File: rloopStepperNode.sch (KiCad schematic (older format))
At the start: 0 parts

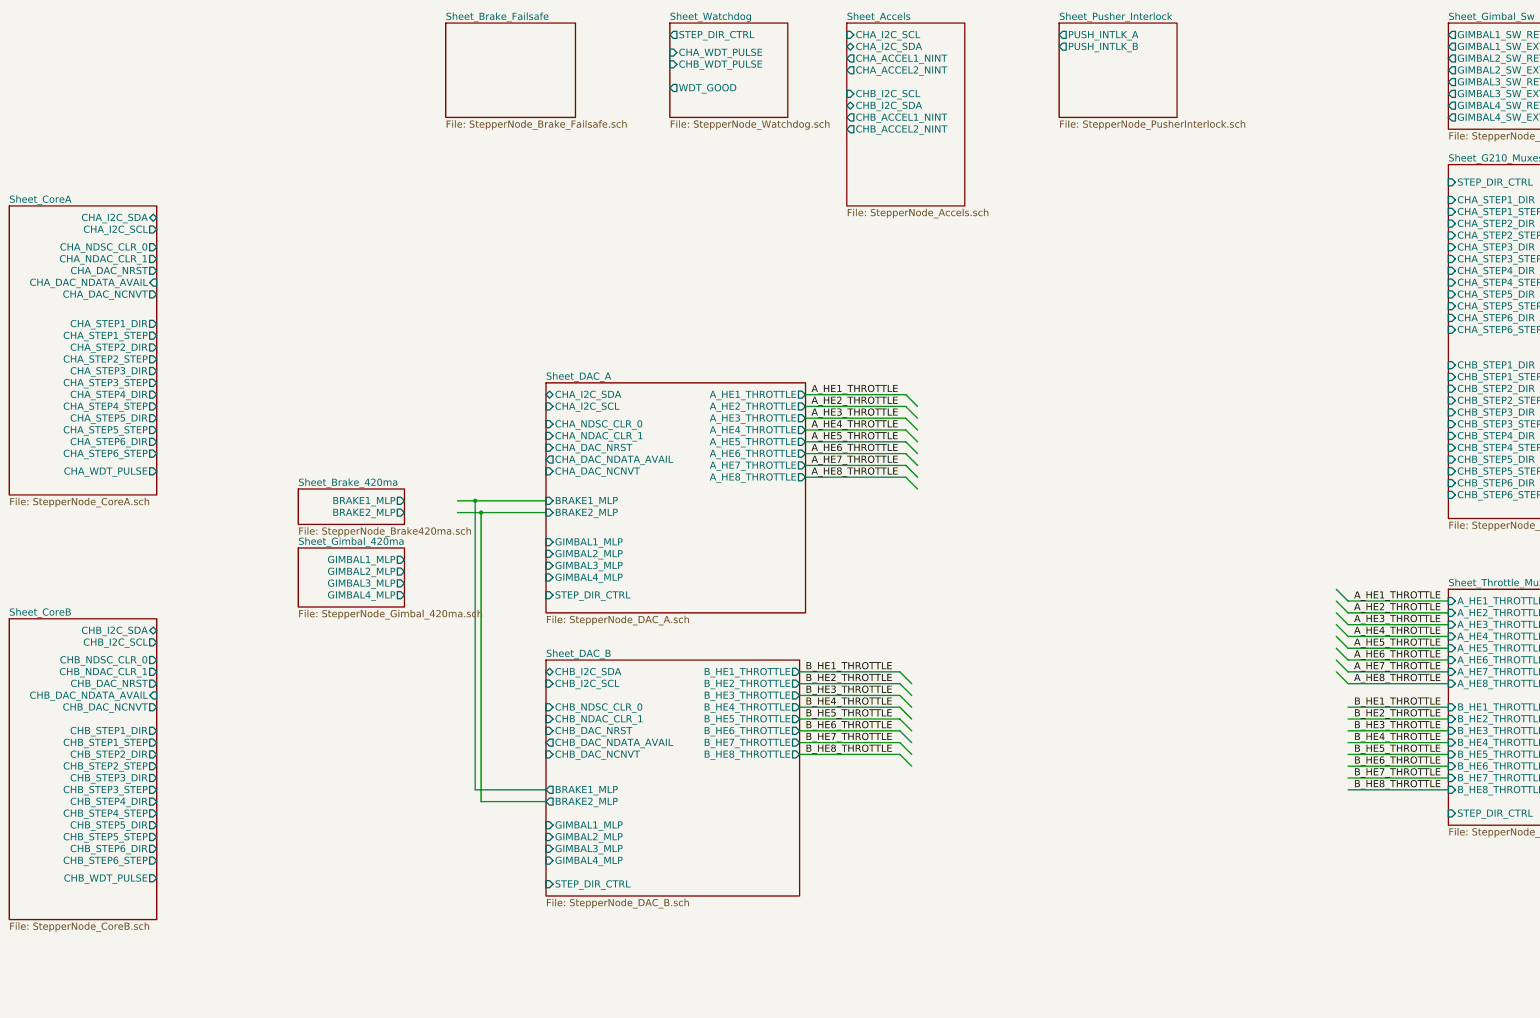
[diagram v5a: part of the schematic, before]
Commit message: Added Aux Prop Interface Sheet
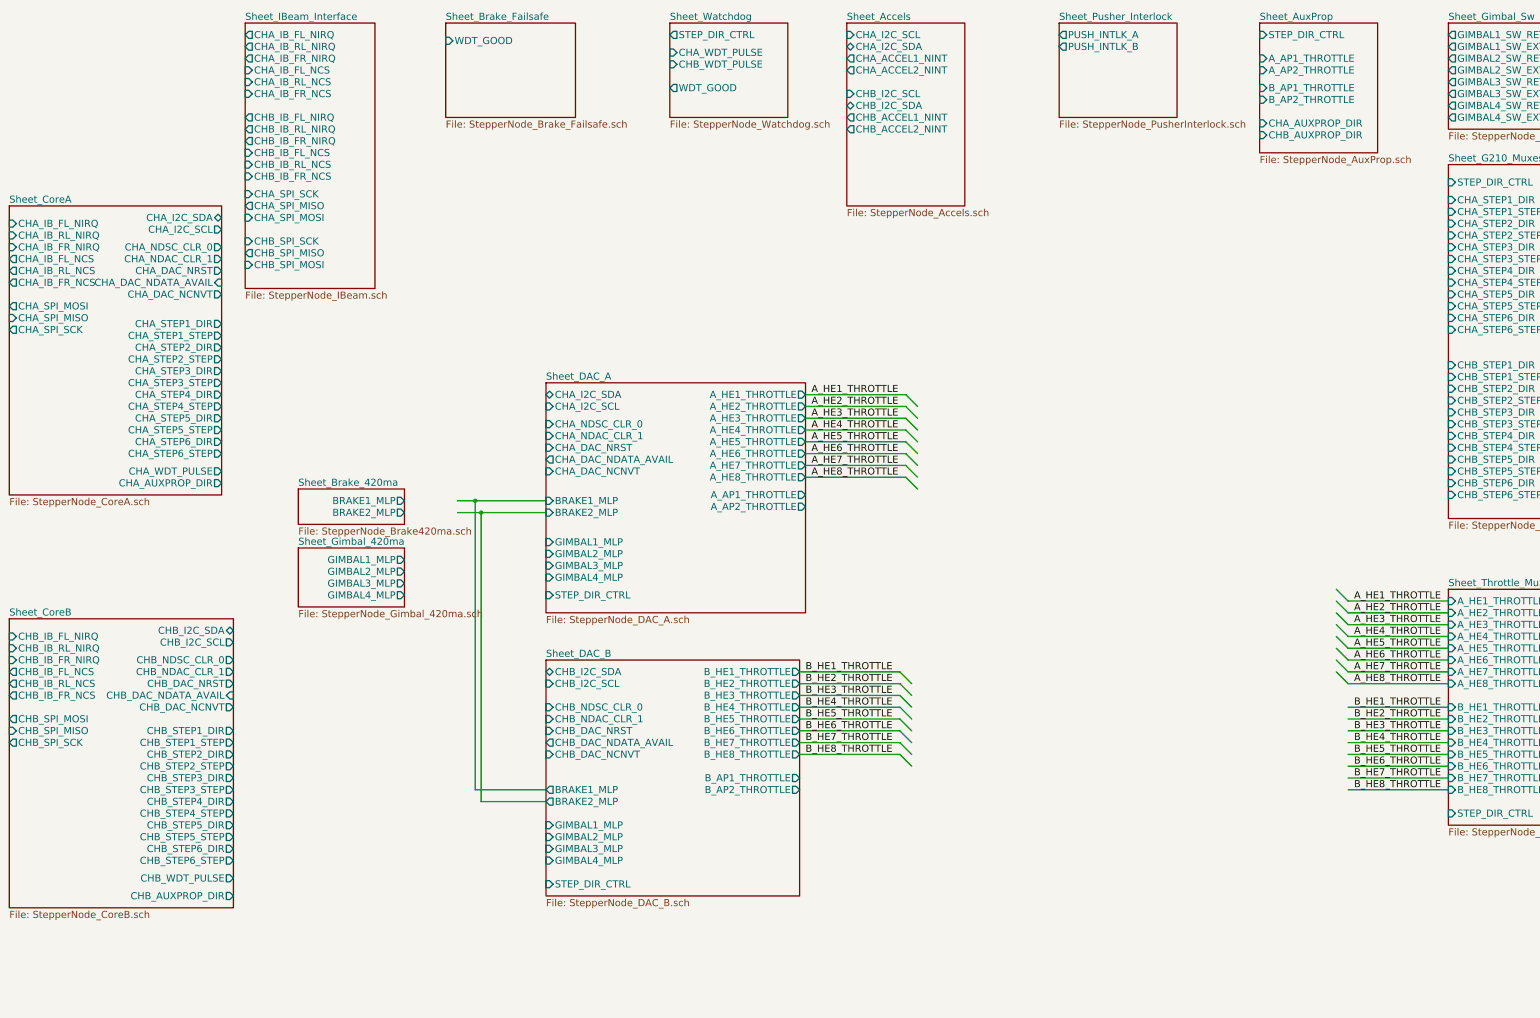
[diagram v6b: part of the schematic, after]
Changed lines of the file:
@@
 $Descr A3 16535 11693
 encoding utf-8
-Sheet 1 14
+Sheet 1 16
 Title "Top Level"
 Date ""
@@
 F22 "GIMBAL4_MLP" I L 6550 5500 60
 F23 "STEP_DIR_CTRL" I L 6550 5650 60
+F24 "A_AP1_THROTTLE" O R 8750 4800 60
+F25 "A_AP2_THROTTLE" O R 8750 4900 60
 $EndSheet
 $Sheet
@@
 F22 "CHB_DAC_NDATA_AVAIL" O L 6550 6900 60
 F23 "CHB_DAC_NCNVT" I L 6550 7000 60
+F24 "B_AP1_THROTTLE" O R 8700 7200 60
+F25 "B_AP2_THROTTLE" O R 8700 7300 60
 $EndSheet
 Wire Wire Line
@@
 $EndSheet
 $Sheet
-S 2000 5850 1250 2550
+S 2000 5850 1900 2450
 U 57556833
 F0 "Sheet_CoreB" 60
 F1 "StepperNode_CoreB.sch" 60
-F2 "CHB_I2C_SDA" B R 3250 5950 60
-F3 "CHB_I2C_SCL" O R 3250 6050 60
-F4 "CHB_NDSC_CLR_0" O R 3250 6200 60
-F5 "CHB_NDAC_CLR_1" O R 3250 6300 60
-F6 "CHB_DAC_NRST" O R 3250 6400 60
-F7 "CHB_DAC_NDATA_AVAIL" I R 3250 6500 60
-F8 "CHB_DAC_NCNVT" O R 3250 6600 60
-F9 "CHB_STEP1_DIR" O R 3250 6800 60
-F10 "CHB_STEP1_STEP" O R 3250 6900 60
-F11 "CHB_STEP2_DIR" O R 3250 7000 60
-F12 "CHB_STEP2_STEP" O R 3250 7100 60
-F13 "CHB_STEP3_DIR" O R 3250 7200 60
-F14 "CHB_STEP3_STEP" O R 3250 7300 60
-F15 "CHB_STEP4_DIR" O R 3250 7400 60
-F16 "CHB_STEP4_STEP" O R 3250 7500 60
-F17 "CHB_STEP5_DIR" O R 3250 7600 60
-F18 "CHB_STEP5_STEP" O R 3250 7700 60
-F19 "CHB_STEP6_DIR" O R 3250 7800 60
-F20 "CHB_STEP6_STEP" O R 3250 7900 60
-F21 "CHB_WDT_PULSE" O R 3250 8050 60
-$EndSheet
-$Sheet
-S 2000 2350 1250 2450
+F2 "CHB_I2C_SDA" B R 3900 5950 60
+F3 "CHB_I2C_SCL" O R 3900 6050 60
+F4 "CHB_NDSC_CLR_0" O R 3900 6200 60
+F5 "CHB_NDAC_CLR_1" O R 3900 6300 60
+F6 "CHB_DAC_NRST" O R 3900 6400 60
+F7 "CHB_DAC_NDATA_AVAIL" I R 3900 6500 60
+F8 "CHB_DAC_NCNVT" O R 3900 6600 60
+F9 "CHB_STEP1_DIR" O R 3900 6800 60
+F10 "CHB_STEP1_STEP" O R 3900 6900 60
+F11 "CHB_STEP2_DIR" O R 3900 7000 60
+F12 "CHB_STEP2_STEP" O R 3900 7100 60
+F13 "CHB_STEP3_DIR" O R 3900 7200 60
+F14 "CHB_STEP3_STEP" O R 3900 7300 60
+F15 "CHB_STEP4_DIR" O R 3900 7400 60
+F16 "CHB_STEP4_STEP" O R 3900 7500 60
+F17 "CHB_STEP5_DIR" O R 3900 7600 60
+F18 "CHB_STEP5_STEP" O R 3900 7700 60
+F19 "CHB_STEP6_DIR" O R 3900 7800 60
+F20 "CHB_STEP6_STEP" O R 3900 7900 60
+F21 "CHB_WDT_PULSE" O R 3900 8050 60
+F22 "CHB_IB_FL_NIRQ" I L 2000 6000 60
+F23 "CHB_IB_RL_NIRQ" I L 2000 6100 60
+F24 "CHB_IB_FR_NIRQ" I L 2000 6200 60
+F25 "CHB_IB_RL_NCS" O L 2000 6400 60
+F26 "CHB_IB_FR_NCS" O L 2000 6500 60
+F27 "CHB_IB_FL_NCS" O L 2000 6300 60
+F28 "CHB_SPI_MOSI" O L 2000 6700 60
+F29 "CHB_SPI_MISO" I L 2000 6800 60
+F30 "CHB_SPI_SCK" O L 2000 6900 60
+F31 "CHB_AUXPROP_DIR" O R 3900 8200 60
+$EndSheet
+$Sheet
+S 2000 2350 1800 2450
 U 57538643
 F0 "Sheet_CoreA" 60
 F1 "StepperNode_CoreA.sch" 60
-F2 "CHA_I2C_SDA" B R 3250 2450 60
-F3 "CHA_I2C_SCL" O R 3250 2550 60
-F4 "CHA_NDSC_CLR_0" O R 3250 2700 60
-F5 "CHA_NDAC_CLR_1" O R 3250 2800 60
-F6 "CHA_DAC_NRST" O R 3250 2900 60
-F7 "CHA_DAC_NDATA_AVAIL" I R 3250 3000 60
-F8 "CHA_DAC_NCNVT" O R 3250 3100 60
-F9 "CHA_STEP1_DIR" O R 3250 3350 60
-F10 "CHA_STEP1_STEP" O R 3250 3450 60
-F11 "CHA_STEP2_DIR" O R 3250 3550 60
-F12 "CHA_STEP2_STEP" O R 3250 3650 60
-F13 "CHA_STEP3_DIR" O R 3250 3750 60
-F14 "CHA_STEP3_STEP" O R 3250 3850 60
-F15 "CHA_STEP4_DIR" O R 3250 3950 60
-F16 "CHA_STEP4_STEP" O R 3250 4050 60
-F17 "CHA_STEP5_DIR" O R 3250 4150 60
-F18 "CHA_STEP5_STEP" O R 3250 4250 60
-F19 "CHA_STEP6_DIR" O R 3250 4350 60
-F20 "CHA_STEP6_STEP" O R 3250 4450 60
-F21 "CHA_WDT_PULSE" O R 3250 4600 60
+F2 "CHA_I2C_SDA" B R 3800 2450 60
+F3 "CHA_I2C_SCL" O R 3800 2550 60
+F4 "CHA_NDSC_CLR_0" O R 3800 2700 60
+F5 "CHA_NDAC_CLR_1" O R 3800 2800 60
+F6 "CHA_DAC_NRST" O R 3800 2900 60
+F7 "CHA_DAC_NDATA_AVAIL" I R 3800 3000 60
+F8 "CHA_DAC_NCNVT" O R 3800 3100 60
+F9 "CHA_STEP1_DIR" O R 3800 3350 60
+F10 "CHA_STEP1_STEP" O R 3800 3450 60
+F11 "CHA_STEP2_DIR" O R 3800 3550 60
+F12 "CHA_STEP2_STEP" O R 3800 3650 60
+F13 "CHA_STEP3_DIR" O R 3800 3750 60
+F14 "CHA_STEP3_STEP" O R 3800 3850 60
+F15 "CHA_STEP4_DIR" O R 3800 3950 60
+F16 "CHA_STEP4_STEP" O R 3800 4050 60
+F17 "CHA_STEP5_DIR" O R 3800 4150 60
+F18 "CHA_STEP5_STEP" O R 3800 4250 60
+F19 "CHA_STEP6_DIR" O R 3800 4350 60
+F20 "CHA_STEP6_STEP" O R 3800 4450 60
+F21 "CHA_WDT_PULSE" O R 3800 4600 60
+F22 "CHA_IB_FL_NIRQ" I L 2000 2500 60
+F23 "CHA_IB_RL_NIRQ" I L 2000 2600 60
+F24 "CHA_IB_FR_NIRQ" I L 2000 2700 60
+F25 "CHA_IB_RL_NCS" O L 2000 2900 60
+F26 "CHA_IB_FR_NCS" O L 2000 3000 60
+F27 "CHA_IB_FL_NCS" O L 2000 2800 60
+F28 "CHA_SPI_MOSI" O L 2000 3200 60
+F29 "CHA_SPI_MISO" I L 2000 3300 60
+F30 "CHA_SPI_SCK" O L 2000 3400 60
+F31 "CHA_AUXPROP_DIR" O R 3800 4700 60
 $EndSheet
 $Sheet
@@
 F0 "Sheet_Brake_Failsafe" 60
 F1 "StepperNode_Brake_Failsafe.sch" 60
+F2 "WDT_GOOD" I L 5700 950 60
+$EndSheet
+$Sheet
+S 4000 800  1100 2250
+U 5753F632
+F0 "Sheet_IBeam_Interface" 60
+F1 "StepperNode_IBeam.sch" 60
+F2 "CHA_IB_FL_NIRQ" O L 4000 900 60
+F3 "CHA_SPI_MOSI" I L 4000 2450 60
+F4 "CHA_SPI_MISO" O L 4000 2350 60
+F5 "CHA_SPI_SCK" I L 4000 2250 60
+F6 "CHA_IB_FL_NCS" I L 4000 1200 60
+F7 "CHA_IB_RL_NIRQ" O L 4000 1000 60
+F8 "CHA_IB_FR_NIRQ" O L 4000 1100 60
+F9 "CHA_IB_RL_NCS" I L 4000 1300 60
+F10 "CHA_IB_FR_NCS" I L 4000 1400 60
+F11 "CHB_IB_FL_NIRQ" O L 4000 1600 60
+F12 "CHB_IB_RL_NIRQ" O L 4000 1700 60
+F13 "CHB_IB_FR_NIRQ" O L 4000 1800 60
+F14 "CHB_IB_RL_NCS" I L 4000 2000 60
+F15 "CHB_IB_FR_NCS" I L 4000 2100 60
+F16 "CHB_IB_FL_NCS" I L 4000 1900 60
+F17 "CHB_SPI_MOSI" I L 4000 2850 60
+F18 "CHB_SPI_MISO" O L 4000 2750 60
+F19 "CHB_SPI_SCK" I L 4000 2650 60
+$EndSheet
+$Sheet
+S 12600 800  1000 1100
+U 575A7A12
+F0 "Sheet_AuxProp" 60
+F1 "StepperNode_AuxProp.sch" 60
+F2 "STEP_DIR_CTRL" I L 12600 900 60
+F3 "A_AP1_THROTTLE" I L 12600 1100 60
+F4 "B_AP1_THROTTLE" I L 12600 1350 60
+F5 "A_AP2_THROTTLE" I L 12600 1200 60
+F6 "B_AP2_THROTTLE" I L 12600 1450 60
+F7 "CHA_AUXPROP_DIR" I L 12600 1650 60
+F8 "CHB_AUXPROP_DIR" I L 12600 1750 60
 $EndSheet
 $EndSCHEMATC

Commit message: Netlist top level
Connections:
- net labels added: A_AP1_THROTTLE, A_AP2_THROTTLE, BRAKE1_MLP, BRAKE2_MLP, B_AP1_THROTTLE, B_AP2_THROTTLE, CHA_ACCEL1_NINT, CHA_ACCEL2_NINT, CHA_AUXPROP_DIR, CHA_DAC_NCNVT, CHA_DAC_NDATA_AVAIL, CHA_DAC_NRST, CHA_I2C_SCL, CHA_I2C_SDA, CHA_IB_FL_NCS, CHA_IB_FL_NIRQ, CHA_IB_FR_NCS, CHA_IB_FR_NIRQ, CHA_IB_RL_NCS, CHA_IB_RL_NIRQ, CHA_NDAC_CLR_1, CHA_NDSC_CLR_0, CHA_SPI_MISO, CHA_SPI_MOSI, CHA_SPI_SCK, CHA_STEP1_DIR, CHA_STEP1_STEP, CHA_STEP2_DIR, CHA_STEP2_STEP, CHA_STEP3_DIR, CHA_STEP3_STEP, CHA_STEP4_DIR, CHA_STEP4_STEP, CHA_STEP5_DIR, CHA_STEP5_STEP, CHA_STEP6_DIR, CHA_STEP6_STEP, CHA_WDT_PULSE, CHB_ACCEL1_NINT, CHB_ACCEL2_NINT, CHB_AUXPROP_DIR, CHB_DAC_NCNVT, CHB_DAC_NDATA_AVAIL, CHB_DAC_NRST, CHB_I2C_SCL, CHB_I2C_SDA, CHB_IB_FL_NCS, CHB_IB_FL_NIRQ, CHB_IB_FR_NCS, CHB_IB_FR_NIRQ, CHB_IB_RL_NCS, CHB_IB_RL_NIRQ, CHB_NDAC_CLR_1, CHB_NDSC_CLR_0, CHB_SPI_MISO, CHB_SPI_MOSI, CHB_SPI_SCK, CHB_STEP1_DIR, CHB_STEP1_STEP, CHB_STEP2_DIR, CHB_STEP2_STEP, CHB_STEP3_DIR, CHB_STEP3_STEP, CHB_STEP4_DIR, CHB_STEP4_STEP, CHB_STEP5_DIR, CHB_STEP5_STEP, CHB_STEP6_DIR, CHB_STEP6_STEP, CHB_WDT_PULSE, GIMBAL1_MLP, GIMBAL1_SW_EXT, GIMBAL1_SW_RET, GIMBAL2_MLP, GIMBAL2_SW_EXT, GIMBAL2_SW_RET, GIMBAL3_MLP, GIMBAL3_SW_EXT, GIMBAL3_SW_RET, GIMBAL4_MLP, GIMBAL4_SW_EXT, GIMBAL4_SW_RET, PUSH_INTLK_A, PUSH_INTLK_B, STEP_DIR_CTRL, WDT_GOOD
- wire segments 38 -> 214
